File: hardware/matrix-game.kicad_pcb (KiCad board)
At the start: 2 copper layers, 100 x 100 mm, 32 parts, among them SW1 button_center, SW2 button_left, SW3 button_down, SW4 button_right, SW5 button_up, U1 NUCLEO-F042K6, U2 MAX7219, U3 DM-OLED096-636

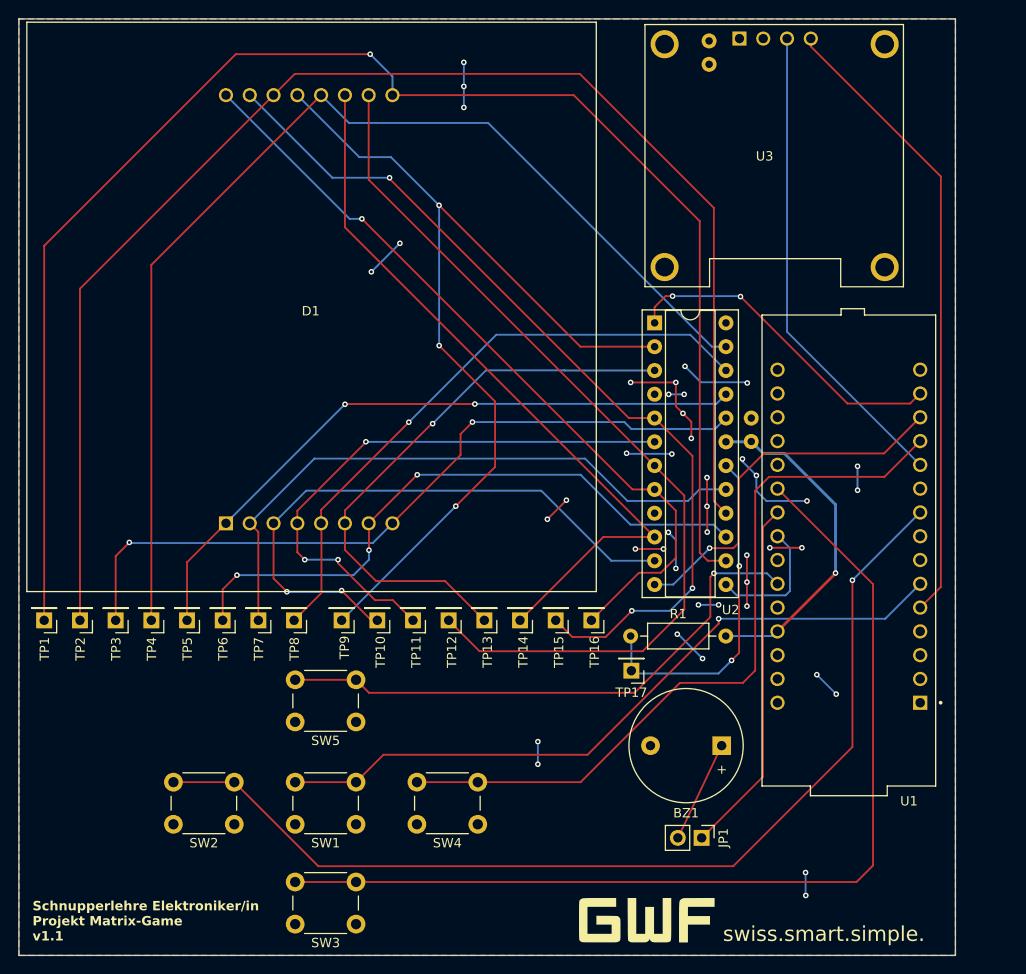
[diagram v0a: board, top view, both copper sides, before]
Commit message: [hardware] Replaced old TP pins with a 1x16, 2.54mm pin header
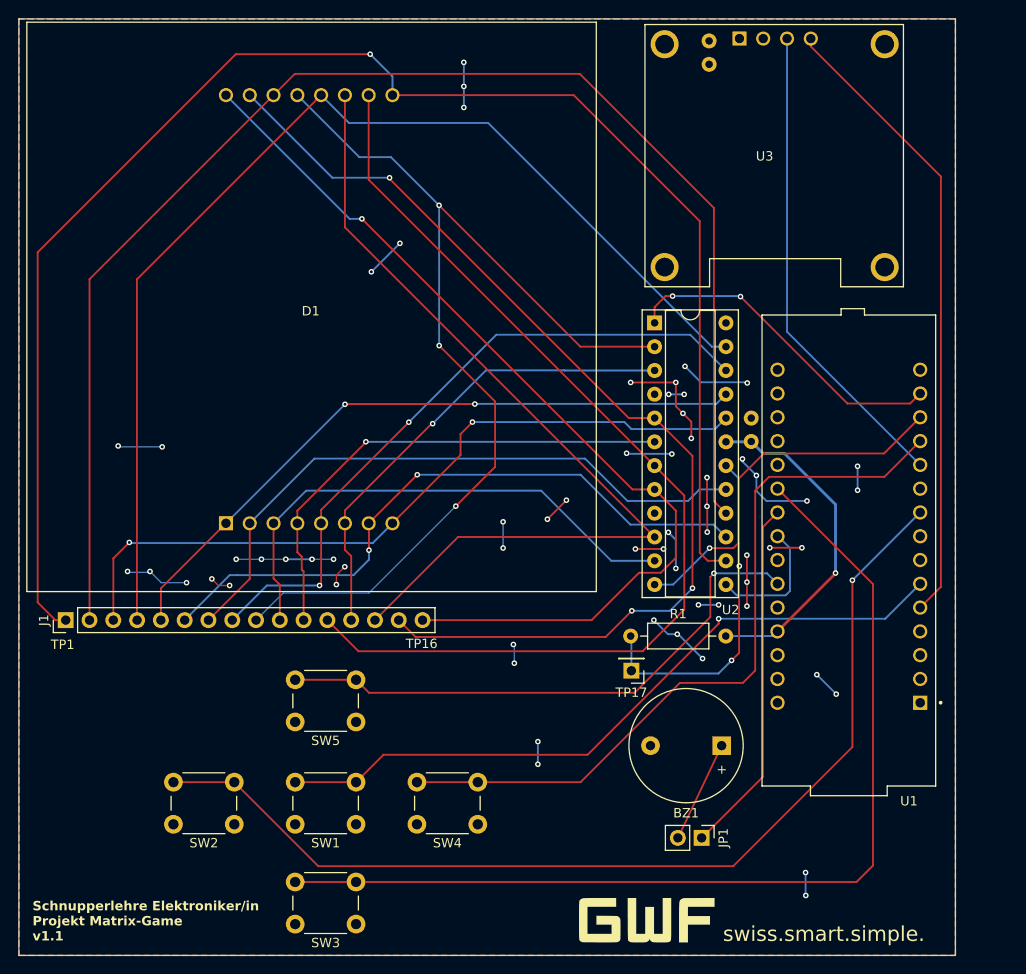
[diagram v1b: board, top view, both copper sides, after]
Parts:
- removed TP1, TP10, TP11, TP12, TP13, TP14, TP15, TP16, TP2, TP3, TP4, TP5, TP6, TP7, TP8, TP9: TestPoint, Connector_PinHeader_2.54mm:PinHeader_1x01_P2.54mm_Vertical
- added J1: Conn_01x16_Pin, Connector_PinHeader_2.54mm:PinHeader_1x16_P2.54mm_Vertical, F.Cu at (95.0, 109.2)
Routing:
- net GND: track 53.5 -> 83.5 mm, vias 28 -> 43
- net Net-(D1-C8): track 83.2 -> 101.3 mm
- net Net-(D1-C7): track 95.0 -> 111.7 mm
- net Net-(D1-C6): track 78.9 -> 94.4 mm
- net Net-(D1-C4): track 97.3 -> 110.2 mm
- net Net-(D1-C5): track 61.5 -> 51.3 mm
- net Net-(D1-C1): track 102.9 -> 112.0 mm
- net Net-(D1-C2): track 64.2 -> 55.9 mm, vias 2 -> 0
- net Net-(D1-C3): track 61.3 -> 53.2 mm, vias 3 -> 1
- net Net-(D1-R8): track 65.6 -> 72.0 mm, vias 1 -> 2
- net +3.3V: track 32.1 -> 36.5 mm, vias 16 -> 20
- net Net-(D1-R1): track 165.6 -> 167.7 mm
- net Net-(D1-R6): track 67.2 -> 69.3 mm, vias 3 -> 2
- net Net-(D1-R7): track 66.8 -> 68.3 mm
- net Net-(D1-R5): track 71.2 -> 72.3 mm
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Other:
- board text added: "TP1"
- board text added: "TP16"

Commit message: [hardware/doc] updated changelog
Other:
- board text added: "Schnupperlehre Elektroniker/in Projekt Matrix-Game ${REVISION}"
- board text removed: "Schnupperlehre Elektroniker/in Projekt Matrix-Game v1.1"
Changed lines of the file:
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@@
 	(title_block
 		(title "Schnupperlehre Elektroniker/in | Projekt Matrix-Game")
-		(date "2025-02-24")
-		(rev "v1.1")
+		(date "2026-08-13")
+		(rev "v1.2")
 		(company "GWF AG")
 		(comment 1 "Timon Burkard")
@@
 		(layer "Edge.Cuts")
 	)
-	(gr_text "Schnupperlehre Elektroniker/in\nProjekt Matrix-Game\nv1.1"
+	(gr_text "Schnupperlehre Elektroniker/in\nProjekt Matrix-Game\n${REVISION}"
 		(at 91.45 143.525 0)
 		(layer "F.SilkS")
